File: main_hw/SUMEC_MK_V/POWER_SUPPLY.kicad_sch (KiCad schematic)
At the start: 34 parts, among them IC1 TPS565242DRLR, J1 XT30PW-M, Q1 Q_PMOS, Q2 Q_PMOS, SW1 SW_DPDT_x2, U1 INA226, U2 AP62301Z6

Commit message: 67yfhtgftu
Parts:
- removed U2: AP62301Z6, Package_TO_SOT_SMD:SOT-563, symbol Regulator_Switching:AP62301WU
- added U7: AP62300Z6, Package_TO_SOT_SMD:SOT-563, symbol Regulator_Switching:AP62300Z6
- renumbered R2 to R1, R3 to R2, R4 to R3, R1 to R4
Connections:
- net +12V: now also U7.1 (VIN)
- net FB_5V: now also U7.6 (FB)
- net GND: now also U7.3 (GND)
- net SW: now also U7.2 (SW)
- net at R6.2, R7.1: now also U7.5 (EN)
- net at C6.2: now also U7.4 (BST)

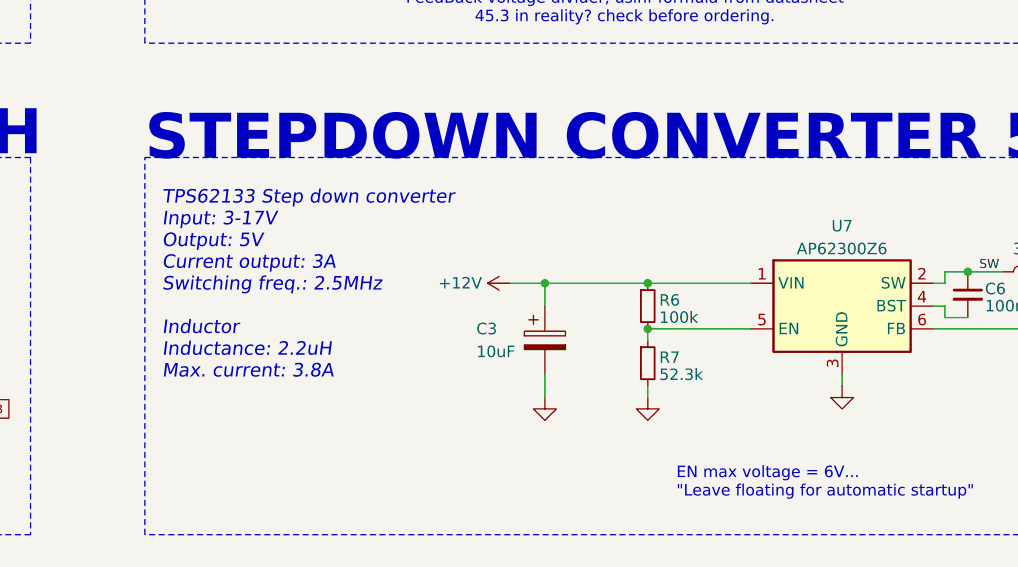
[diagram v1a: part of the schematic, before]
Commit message: MK5 bugfix fixed POL_L, minor changes, deleted nSLEEP and nFault connections to the MCU
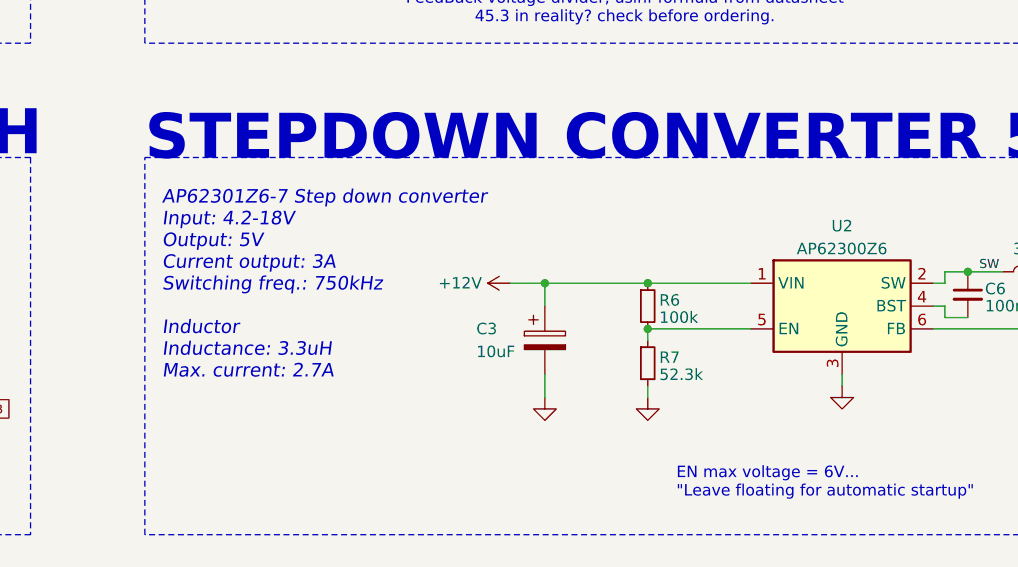
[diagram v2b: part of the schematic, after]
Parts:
- renumbered U7 to U2
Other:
- note added: "AP62301Z6-7 Step down converter Input: 4.2-18V Output: 5V Current output: 3A Switching freq.: 750kHz Inductor Inductance: 3.3uH Max. current: 2.7A"
- note removed: "TPS62133 Step down converter Input: 3-17V Output: 5V Current output: 3A Switching freq.: 2.5MHz Inductor Inductance: 2.2uH Max. current: 3.8A"

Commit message: MK5 changes and deletion of useless files
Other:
- note removed: "4A?"
- note removed: "EN max voltage = 6V... "Leave floating for automatic startup""
- note removed: "FeedBack voltage divider, usinf formula from datasheet 45.3 in reality? check before ordering."
- note removed: "will 0805 resistor be sufficent?"
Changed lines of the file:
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@@
 		)
 	)
-	(text "4A?"
-		(exclude_from_sim no)
-		(at 45.085 158.75 0)
-		(effects
-			(font
-				(size 1.27 1.27)
-			)
-		)
-	)
-	(text "FeedBack voltage divider, usinf formula from datasheet\n45.3 in reality? check before ordering. "
-		(exclude_from_sim no)
-		(at 168.91 60.96 0)
-		(effects
-			(font
-				(size 1.27 1.27)
-			)
-		)
-	)
-	(text "will 0805 resistor be sufficent?"
-		(exclude_from_sim no)
-		(at 46.355 167.64 0)
-		(effects
-			(font
-				(size 1.27 1.27)
-			)
-		)
-	)
-	(text "EN max voltage = 6V...\n\"Leave floating for automatic startup\""
-		(exclude_from_sim no)
-		(at 174.625 113.665 0)
-		(effects
-			(font
-				(size 1.27 1.27)
-			)
-			(justify left)
-		)
-	)
 	(junction
 		(at 241.3 90.17)
@@
 			"AAAAAAAAAAAAAAAAAAAAAAAAAAAAAAAAAAAAAAAAAAAAAAAAAAAAAAAAAAAAAAAAAAAAAAAAAAAA"
 			"AAAAAAAAAAAAAAAAAAAAAAAAAAAAAAAAAAAAAAAAAAAAAAAAAAAAAAAAAAAAAAAAAAAAAAAAAAAA"
+			"AAAAAAAAAAAAAAAAAAAAAAAAAAAAAAAAAAAAAAAAAAAAAAAAAAAAAAAAAAAAAAAAAAAAAAAAAAAA"
+			"AAAAAAAAAAAAAAAAAAAAAAAAAAAAAAAAAAAAAAAAAAAAAAAAAAAAAAAAAAAAAAAAAAAAAAAAAAAA"
+			"AAAAAAAAAAAAAAAAAAAAAAAAAAAAAAAAAAAAAAAAAAAAAAAAAAAAAAAAAAAAAAAAAAAAAAAAAAAA"
+			"AAAAAAAAAAAAAAAAAAAAAAAAAAAAAAAAAAAAAAAAAAAAAAAAAAAAAAAAAAAAAAAAAAAAAAAAAAAA"
+			"AAAAAAAAAAAAAAAAAAAAAAAAAAAAAAAAAAAAAAAAAAAAAAAAAAAAAAAAAAAAAAAAAAAAAAAAAAAA"
+			"AAAAAAAAAAAAAAAAAAAAAAAAAAAAAAAAAAAAAAAAAAAAAAAAAAAAAAAAAAAAAAAAAAAAAAAAAAAA"
+			"AAAAAAAAAAAAAAAAAAAAAAAAAAAAAAAAAAAAAAAAAAAAAAAAAAAAAAAAAAAAAAAAAAAAAAAAAAAA"
+			"AAAAAAAAAAAAAAAAAAAAAAAAAAAAAAAAAAAAAAAAAAAAAAAAAAAAAAAAAAAAAAAAAAAAAAAAAAAA"
+			"AAAAAAAAAAAAAAAAAAAAAAAAAAAAAAAAAAAAAAAAAAAAAAAAAAAAAAAAAAAAAAAAAAAAAAAAAAAA"
+			"AAAAAAAAAAAAAAAAAAAAAAAAAAAAAAAAAAAAAAAAAAAAAAAAAAAAAAAAAAAAAAAAAAAAAAAAAAAA"
+			"AAAAAAAAAAAAAAAAAAAAAAAAAAAAAAAAAAAAAAAAAAAAAAAAAAAAAAAAAAAAAAAAAAAAAAAAAAAA"
+			"AAAAAAAAAAAAAAAAAAAAAAAAAAAAAAAAAAAAAAAAAAAAAAAAAAAAAAAAAAAAAAAAAAAAAAAAAAAA"
+			"AAAAAAAAAAAAAAAAAAAAAAAAAAAAAAAAAAAAAAAAAAAAAAAAAAAAAAAAAAAAAAAAAAAAAAAAAAAA"
+			"AAAAAAAAAAAAAAAAAAAAAAAAAAAAAAAAAAAAAAAAAAAAAAAAAAAAAAAAAAAAAAAAAAAAAAAAAAAA"
+			"AAAAAAAAAAAAAAAAAAAAAAAAAAAAAAAAAAAAAAAAAAAAAAAAAAAAAAAAAAAAAAAAAAAAAAAAAAAA"
+			"AAAAAAAAAAAAAAAAAAAAAAAAAAAAAAAAAAAAAAAAAAAAAAAAAAAAAAAAAAAAAAAAAAAAAAAAAAAA"
+			"AAAAAAAAAAAAAAAAAAAAAAAAAAAAAAAAAAAAAAAAAAAAAAAAAAAAAAAAAAAAAAAAAAAAAAAAAAAA"
+			"AAAAAAAAAAAAAAAAAAAAAAAAAAAAAAAAAAAAAAAAAAAAAAAAAAAAAAAAAAAAAAAAAAAAAAAAAAAA"
 			"AAAAAAAAAAAAAAAAAA=="
 		)
@@
 			"QQBBAEEAQQBBAEEAQQBBAEEAQQBBAEEAQQBBAEEAQQBBAEEAQQBBAEEAQQBBAEEAQQBBAEEAQQBB"
 			"AEEAQQBBAEEAQQBBAEEAQQBBAEEAQQBBAEEAQQBBAEEAQQBBAEEAQQBBAEEAQQBBAEEAQQBBAEEA"
+			"QQBBAEEAQQBBAEEAQQBBAEEAQQBBAEEAQQBBAEEAQQBBAEEAQQBBAEEAQQBBAEEAQQBBAEEAQQBB"
+			"AEEAQQBBAEEAQQBBAEEAQQBBAEEAQQBBAEEAQQBBAEEAQQBBAEEAQQBBAEEAQQBBAEEAQQBBAEEA"
+			"QQBBAEEAQQBBAEEAQQBBAEEAQQBBAEEAQQBBAEEAQQBBAEEAQQBBAEEAQQBBAEEAQQBBAEEAQQBB"
+			"AEEAQQBBAEEAQQBBAEEAQQBBAEEAQQBBAEEAQQBBAEEAQQBBAEEAQQBBAEEAQQBBAEEAQQBBAEEA"
+			"QQBBAEEAQQBBAEEAQQBBAEEAQQBBAEEAQQBBAEEAQQBBAEEAQQBBAEEAQQBBAEEAQQBBAEEAQQBB"
+			"AEEAQQBBAEEAQQBBAEEAQQBBAEEAQQBBAEEAQQBBAEEAQQBBAEEAQQBBAEEAQQBBAEEAQQBBAEEA"
+			"QQBBAEEAQQBBAEEAQQBBAEEAQQBBAEEAQQBBAEEAQQBBAEEAQQBBAEEAQQBBAEEAQQBBAEEAQQBB"
+			"AEEAQQBBAEEAQQBBAEEAQQBBAEEAQQBBAEEAQQBBAEEAQQBBAEEAQQBBAEEAQQBBAEEAQQBBAEEA"
+			"QQBBAEEAQQBBAEEAQQBBAEEAQQBBAEEAQQBBAEEAQQBBAEEAQQBBAEEAQQBBAEEAQQBBAEEAQQBB"
+			"AEEAQQBBAEEAQQBBAEEAQQBBAEEAQQBBAEEAQQBBAEEAQQBBAEEAQQBBAEEAQQBBAEEAQQBBAEEA"
+			"QQBBAEEAQQBBAEEAQQBBAEEAQQBBAEEAQQBBAEEAQQBBAEEAQQBBAEEAQQBBAEEAQQBBAEEAQQBB"
+			"AEEAQQBBAEEAQQBBAEEAQQBBAEEAQQBBAEEAQQBBAEEAQQBBAEEAQQBBAEEAQQBBAEEAQQBBAEEA"
+			"QQBBAEEAQQBBAEEAQQBBAEEAQQBBAEEAQQBBAEEAQQBBAEEAQQBBAEEAQQBBAEEAQQBBAEEAQQBB"
+			"AEEAQQBBAEEAQQBBAEEAQQBBAEEAQQBBAEEAQQBBAEEAQQBBAEEAQQBBAEEAQQBBAEEAQQBBAEEA"
+			"QQBBAEEAQQBBAEEAQQBBAEEAQQBBAEEAQQBBAEEAQQBBAEEAQQBBAEEAQQBBAEEAQQBBAEEAQQBB"
+			"AEEAQQBBAEEAQQBBAEEAQQBBAEEAQQBBAEEAQQBBAEEAQQBBAEEAQQBBAEEAQQBBAEEAQQBBAEEA"
+			"QQBBAEEAQQBBAEEAQQBBAEEAQQBBAEEAQQBBAEEAQQBBAEEAQQBBAEEAQQBBAEEAQQBBAEEAQQBB"
+			"AEEAQQBBAEEAQQBBAEEAQQBBAEEAQQBBAEEAQQBBAEEAQQBBAEEAQQBBAEEAQQBBAEEAQQBBAEEA"
 			"QQBBAEEAQQBBAEEAQQBBAEEAQQBBAEEAQQBBAEEAQQBBAEEAQQBBAA=="
 		)
@@
 			"AAAAAAAAAAAAAAAAAAAAAAAAAAAAAAAAAAAAAAAAAAAAAAAAAAAAAAAAAAAAAAAAAAAAAAAAAAAA"
 			"AAAAAAAAAAAAAAAAAAAAAAAAAAAAAAAAAAAAAAAAAAAAAAAAAAAAAAAAAAAAAAAAAAAAAAAAAAAA"
+			"AAAAAAAAAAAAAAAAAAAAAAAAAAAAAAAAAAAAAAAAAAAAAAAAAAAAAAAAAAAAAAAAAAAAAAAAAAAA"
+			"AAAAAAAAAAAAAAAAAAAAAAAAAAAAAAAAAAAAAAAAAAAAAAAAAAAAAAAAAAAAAAAAAAAAAAAAAAAA"
+			"AAAAAAAAAAAAAAAAAAAAAAAAAAAAAAAAAAAAAAAAAAAAAAAAAAAAAAAAAAAAAAAAAAAAAAAAAAAA"
+			"AAAAAAAAAAAAAAAAAAAAAAAAAAAAAAAAAAAAAAAAAAAAAAAAAAAAAAAAAAAAAAAAAAAAAAAAAAAA"
+			"AAAAAAAAAAAAAAAAAAAAAAAAAAAAAAAAAAAAAAAAAAAAAAAAAAAAAAAAAAAAAAAAAAAAAAAAAAAA"
+			"AAAAAAAAAAAAAAAAAAAAAAAAAAAAAAAAAAAAAAAAAAAAAAAAAAAAAAAAAAAAAAAAAAAAAAAAAAAA"
+			"AAAAAAAAAAAAAAAAAAAAAAAAAAAAAAAAAAAAAAAAAAAAAAAAAAAAAAAAAAAAAAAAAAAAAAAAAAAA"
+			"AAAAAAAAAAAAAAAAAAAAAAAAAAAAAAAAAAAAAAAAAAAAAAAAAAAAAAAAAAAAAAAAAAAAAAAAAAAA"
+			"AAAAAAAAAAAAAAAAAAAAAAAAAAAAAAAAAAAAAAAAAAAAAAAAAAAAAAAAAAAAAAAAAAAAAAAAAAAA"
+			"AAAAAAAAAAAAAAAAAAAAAAAAAAAAAAAAAAAAAAAAAAAAAAAAAAAAAAAAAAAAAAAAAAAAAAAAAAAA"
+			"AAAAAAAAAAAAAAAAAAAAAAAAAAAAAAAAAAAAAAAAAAAAAAAAAAAAAAAAAAAAAAAAAAAAAAAAAAAA"
+			"AAAAAAAAAAAAAAAAAAAAAAAAAAAAAAAAAAAAAAAAAAAAAAAAAAAAAAAAAAAAAAAAAAAAAAAAAAAA"
+			"AAAAAAAAAAAAAAAAAAAAAAAAAAAAAAAAAAAAAAAAAAAAAAAAAAAAAAAAAAAAAAAAAAAAAAAAAAAA"
+			"AAAAAAAAAAAAAAAAAAAAAAAAAAAAAAAAAAAAAAAAAAAAAAAAAAAAAAAAAAAAAAAAAAAAAAAAAAAA"
+			"AAAAAAAAAAAAAAAAAAAAAAAAAAAAAAAAAAAAAAAAAAAAAAAAAAAAAAAAAAAAAAAAAAAAAAAAAAAA"
+			"AAAAAAAAAAAAAAAAAAAAAAAAAAAAAAAAAAAAAAAAAAAAAAAAAAAAAAAAAAAAAAAAAAAAAAAAAAAA"
+			"AAAAAAAAAAAAAAAAAAAAAAAAAAAAAAAAAAAAAAAAAAAAAAAAAAAAAAAAAAAAAAAAAAAAAAAAAAAA"
+			"AAAAAAAAAAAAAAAAAAAAAAAAAAAAAAAAAAAAAAAAAAAAAAAAAAAAAAAAAAAAAAAAAAAAAAAAAAAA"
 			"AAAAAAAAAAAAAAAAAAAAAAAAAAAAAAAAAA=="
 		)
@@
 			"AGYAbwBtADAAOABOAC8AKwBnAFEAdAAyAFUAVABqAGoANAB6AHIARgA5AHcAUQBhAHQAUAB2AGsA"
 			"UwA3AFUAbwBhADUAVgBlAFgAUgA2ADgATgBQAE0AVwBEAHcAUwBJAHkAWgBOAEEATwB6AHYAKwBt"
-			"AEwASwBnAEMAQQBMAEYAdwArAGUAUgA1AFAAZABJAGIARgBxAE8AcQBnAC8ANABlAFIAOABEAA=="
+			"AEwASwBnAEMAQQBMAEYAdwArAGUAUgA1AFAAZABJAGIARgBxAE8AcQBnAC8ANABlAFIAOABEAAAA"
+			"AACQY2JPfgIAAAEAAAAAAAAAAAAAAAAAAACdqX5jAKYEgAAAAAAAAAAAAwAAAAAAAAAQ82FPfgIA"
+			"AAEAAAAAAAAAAAAAAAAAAACYqXtjAKcEgAAAAAAAAAAABAAAAAAAAAAAAAAAAAAAAAEAAAAAAAAA"
+			"AAAAAAAAAACXqXhjAKgEgAAAAAAAAAAABAAAAAAAAAAAAAAAAAAAAAEAAAAAAAAAAAAAAAAAAACS"
+			"qXVjAKkEgAAAAAAAAAAAAwAAAAAAAABg62FPfgIAAAEAAAAAAAAAAAAAAAAAAACRqXJjAKoEgAAA"
+			"AAAAAAAAAwAAAAAAAADQVmNPfgIAAAEAAAAAAAAAAAAAAAAAAACMqW9jAKsEgAAAAAAAAAAAAwAA"
+			"AAAAAABwZmJPfgIAAAEAAAAAAAAAAAAAAAAAAACLqWxjAKwEgEM6L1dJTkRPV1MvZm9udHNcc21h"
+			"bGxlZy5mb24AAAAAAAAAAAAAAACGqWljAK0EgEM6L1dJTkRPV1MvZm9udHNcc21hbGxmZS5mb24A"
+			"AAAAAAAAAAAAAACFqWZjAK4EgAAAAAAAAAAACAAAAAAAAAAw9ztPfgIAAAEAAAAAAAAAAAAAAAAA"
+			"AACAqWNjAK8EgAAAAAAAAAAABAAAAAAAAAAAAAAAAAAAAAEAAAAAAAAAAAAAAAAAAAC/qWBjALAE"
+			"gAAAAAAAAAAACAAAAAAAAADw/jtPfgIAAAEAAAAAAAAAAAAAAAAAAAC6qV1jALEEgAAAAAAAAAAA"
+			"CAAAAAAAAABw9ztPfgIAAAEAAAAAAAAAAAAAAAAAAAC5qVpjALIEgAAAAAAAAAAAAwAAAAAAAAAA"
+			"VWNPfgIAAAEAAAAAAAAAAAAAAAAAAAC0qVdjALMEgAAAAAAAAAAAAwAAAAAAAABg8WFPfgIAAAEA"
+			"AAAAAAAAAAAAAAAAAACzqVRjALQEgAAAAAAAAAAAAwAAAAAAAABQY2JPfgIAAAEAAAAAAAAAAAAA"
+			"AAAAAACuqVFjALUEgEM6L1dJTkRPV1MvZm9udHNcc21hbGxmci5mb24AAAAAAAAAAAAAAACtqU5j"
+			"ALYEgAAAAAAAAAAAAwAAAAAAAACgV2NPfgIAAAEAAAAAAAAAAAAAAAAAAACoqUtjALcEgAAAAAAA"
+			"AAAABAAAAAAAAAAAAAAAAAAAAAEAAAAAAAAAAAAAAAAAAACnqUhjALgEgAAAAAAAAAAAAwAAAAAA"
+			"AADgV2NPfgIAAAEAAAAAAAAAAAAAAAAAAACiqUVjALkEgAAAAAAAAAAAAwAAAAAAAABwWGNPfgIA"
+			"AAEAAAAAAAAAAAAAAAAAAAChqUJjALoEgAAAAAAAAAAABAAAAAAAAAAAAAAAAAAAAAEAAAAAAA=="
 		)
 	)
@@
 			"QgBoAEEARwBnAEEAYwBRAEIASgBBAEQAQQBBAFEAUQBCAGkAQQBIAFUAQQBVAGcAQQB4AEEARQB3"
 			"AEEAWgBnAEEAMwBBAEQAWQBBAFkAZwBBAHYAQQBHAGMAQQBVAHcAQgAyAEEARwBZAEEAVABRAEIA"
-			"bABBAEQARQBBAGUAUQBCAFgAQQ=="
+			"bABBAEQARQBBAGUAUQBCAFgAQVVGQlFVRkJRVUZCUVVGQlFVRkJRVUZCUVVGQlFVRkJRVUZCUVVG"
+			"QlFVRkJRVUZCUVVGQlFVRkJRVUZCUVVGQlFVRkJRVUZCUVVGQlFVRkJRVUZCUVVGQlFVRkJRVUZC"
+			"UVVGQlFVRkJRVUZCUVVGQlFVRkJRVUZCUVVGQlFVRkJRVUZCUVVGQlFVRkJRVUZCUVVGQlFVRkJR"
+			"VUZCUVVGQlFVRkJRVUZCUVVGQlFVRkJRVUZCUVVGQlFVRkJRVUZCUVVGQlFVRkJRVUZCUVVGQlFV"
+			"RkJRVUZCUVVGQlFVRkJRVUZCUVVGQlFVRkJRVUZCUVVGQlFVRkJRVUZCUVVGQlFVRkJRVUZCUVVG"
+			"QlFVRkJRVUZCUVVGQlFVRkJRVUZCUVVGQlFVRkJRVUZCUVVGQlFVRkJRVUZCUVVGQlFVRkJRVUZC"
+			"UVVGQlFVRkJRVUZCUVVGQlFVRkJRVUZCUVVGQlFVRkJRVUZCUVVGQlFacTg1NlFBdEFTQUFBQUFB"
+			"QUFBQUFBZWlhb2VBQUFBQUJEWS9FbU1BUUFBWkx6bHBBQzFCSUFHQUFBQUVBQUFBTkRYK3YvLy8v"
+			"Ly9BQUFBQUFBQUFBQm12QnVrQUxZRWdGUmxjbTFwYm1Gc0FBQUFBQUFBQUFBQUFBQUFBQUFBQUdD"
+			"OEdhUUF0d1NBVUcvRm9XVjJibThBQUFBQUFBQUFBQUFBQUFBQUFBQUFZcndmcEFDNEJJQk9aV2R5"
+			"YVhSaElFTjFjbk5wZG1FQUFBQUFBQUFBQUFCc3ZCMmtBTGtFZ0V0aGJNU3hiaURFc0hSaGJHbHJB"
+			"QUFBQUFBQUFBQUFBRzY4RTZRQXVnU0FSc09wYkd2RHRuYkRxWElBQUFBQUFBQUFBQUFBQUFBQWFM"
+			"d1JwQUM3QklBQUFBQUFBQUFBQUtsVG9vQUFBQUFBa05YOFNZd0JBQUJxdkJla0FMd0VnR3QxY25y"
+			"RHJYWmhBQUFBQUFBQUFBQUFBQUFBQUFBQUFIUzhGYVFBdlFTQVFtOXNaQ0JKZEdGc2FXTUFBQUFB"
+			"QUFBQUFBQUFBQUFBZHJ3THBBQytCSURRbjlDKzBMdlJnOUMyMExqUmdOQzkwWXZRdVFBQUFBQnd2"
+			"QW1rQUw4RWdBWUFBQUFRQUFBQW9NYjYvLy8vLy84QUFBQUFBQUFBQUhLOEQ2UUF3QVNBQUFBQUFB"
+			"QUFBQURlNjNCMkFBQUFBQkRmL0VtTUFRQUFmTHdOcEFEQkJJQnc0L3hKakFFQUFOK2ZMNjhBQUFB"
+			"QTBOdjhTWXdCQUFCK3ZBT2tBTUlFZ0VsVFQwTlFNMTlKVmpVd0FBQUFBQUFBQUFBQUFBQUFBSGk4"
+			"QWFRQXd3U0FBQUFBQUFBQUFBRA=="
 		)
 	)

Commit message: schematic fixes
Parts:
- removed C2: 100nF, Capacitor_SMD:C_0805_2012Metric_Pad1.18x1.45mm_HandSolder, symbol Device:C
- removed Q1: Q_PMOS, Package_TO_SOT_SMD:SOT-23-3, symbol Device:Q_PMOS_GSD
- removed R2: 10k, Resistor_SMD:R_0805_2012Metric_Pad1.20x1.40mm_HandSolder, symbol Device:R
- added D?: D, symbol Device:D
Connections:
- net +5V: now also D?.1 (K); no longer D2.1 (K)
- net VBUS_USB: now also D?.2 (A); no longer D2.2 (A)
- net VOUT_5V: now also D1.2 (A)
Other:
- moved on the sheet: D1, D2

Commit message: updates to mk5
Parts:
- gave numbers to parts that had none: 1
- renumbered C11 to C10, C12 to C11, C3 to C2, C4 to C3, C5 to C4, C6 to C5, C7 to C6, C8 to C7, C9 to C8, C10 to C9, Q2 to Q1, R3 to R2, R4 to R3, R5 to R4, R6 to R5, R7 to R6, R8 to R7, R9 to R8, R10 to R9
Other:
- note removed: "SWITCHING SIMULATION - FALSTAD"
- moved on the sheet: D2
